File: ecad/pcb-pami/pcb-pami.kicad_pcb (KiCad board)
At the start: 4 copper layers, 95 x 95 mm, 85 parts, among them J1 USB_C_Receptacle_USB2.0_16P, J10 Conn_01x02_Pin, J11 Conn_01x05_Pin, J12 Conn_01x02_Pin, J13 Conn_01x04_Pin, J14 Conn_01x04_Pin, J15 Conn_01x02_Pin, J16 Conn_01x05_Pin, J17 Conn_01x07_Pin, J2 Conn_01x11_Socket, J21 Conn_01x05_Pin, J22 Conn_01x04_Pin, J23 Conn_01x03_Pin, J26 Conn_01x03_Pin, J27 Conn_01x02_Pin, J3 Conn_01x08_Socket, J4 Conn_01x11_Socket, J5 Conn_01x02_Pin, J6 Conn_01x02_Pin, J7 Conn_01x02_Pin, J8 Conn_01x03_Pin, J9 Conn_01x02_Pin, SW1 SW_Push, SW2 SW_Push, U10 MCP23008-xSO, U2 LTC4412xS6, U3 LTC4412xS6, U4 AMS1117-3.3 (UMW), U6 ESP32-S3-WROOM-1, U7 TMC2209_SILENTSTEPSTICK, U8 TMC2209_SILENTSTEPSTICK, U9 TMC2209_SILENTSTEPSTICK

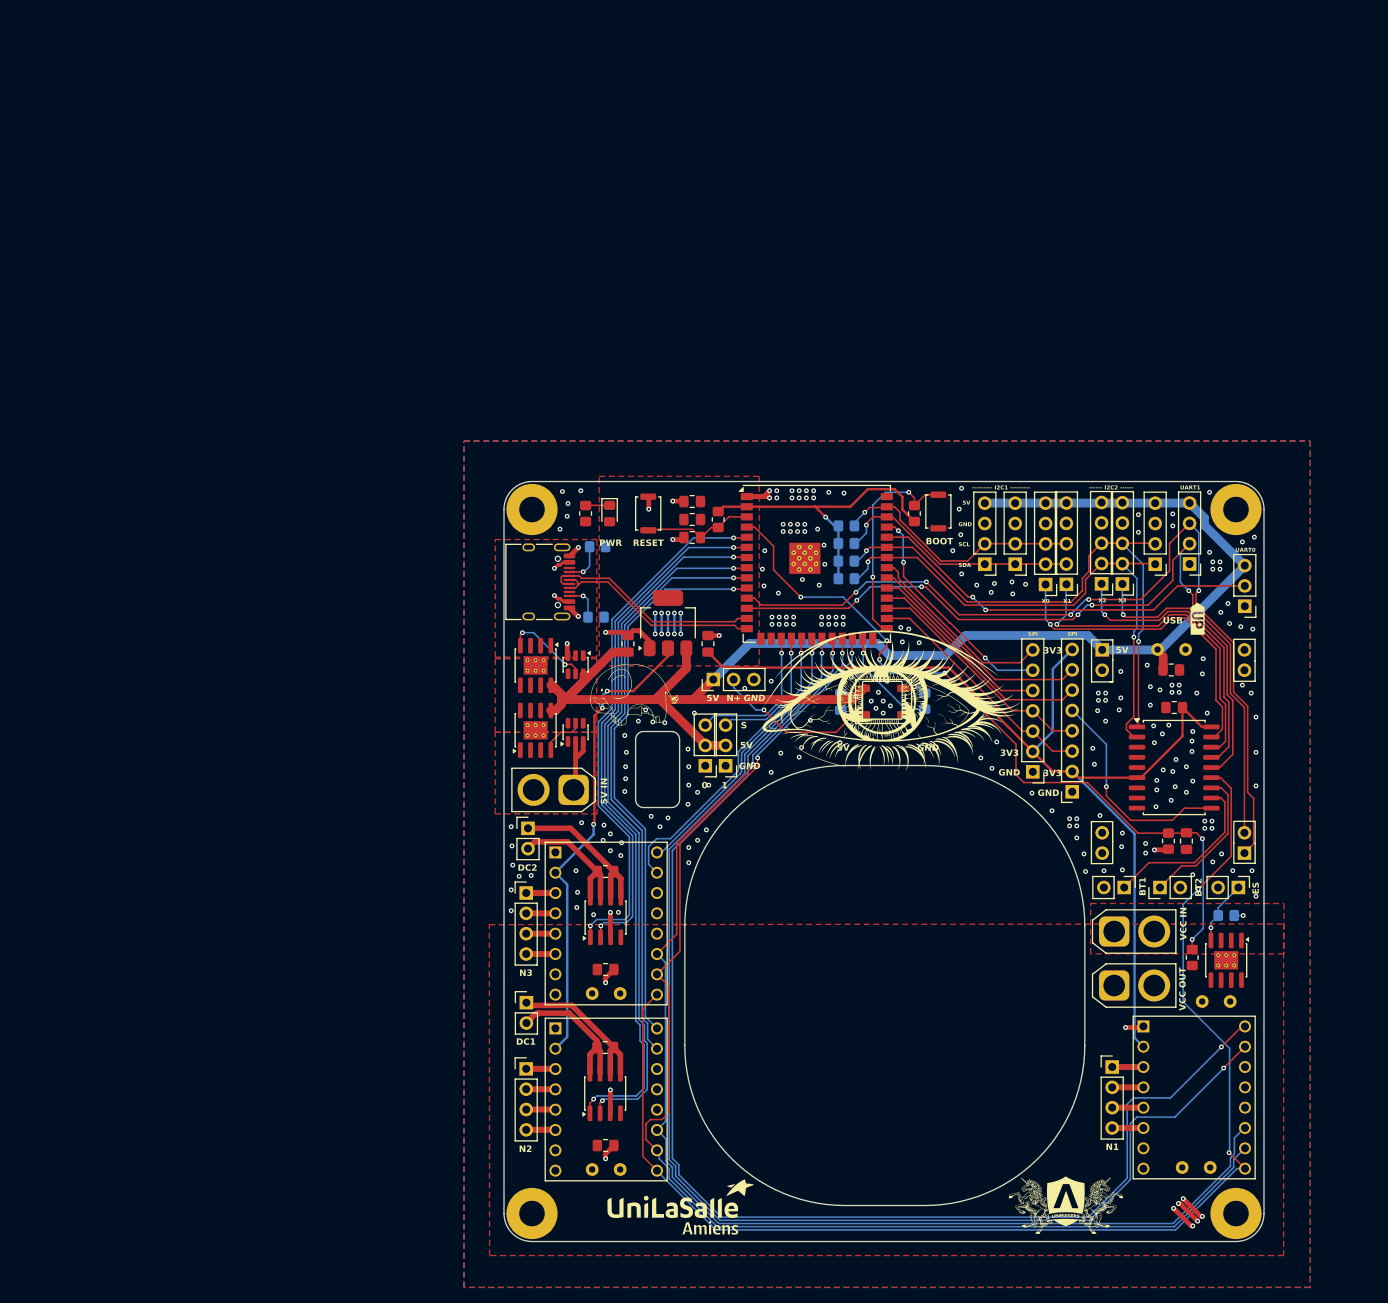
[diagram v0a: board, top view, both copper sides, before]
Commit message: [ECAD] debut nouvelle carte, [FW] generation strat web
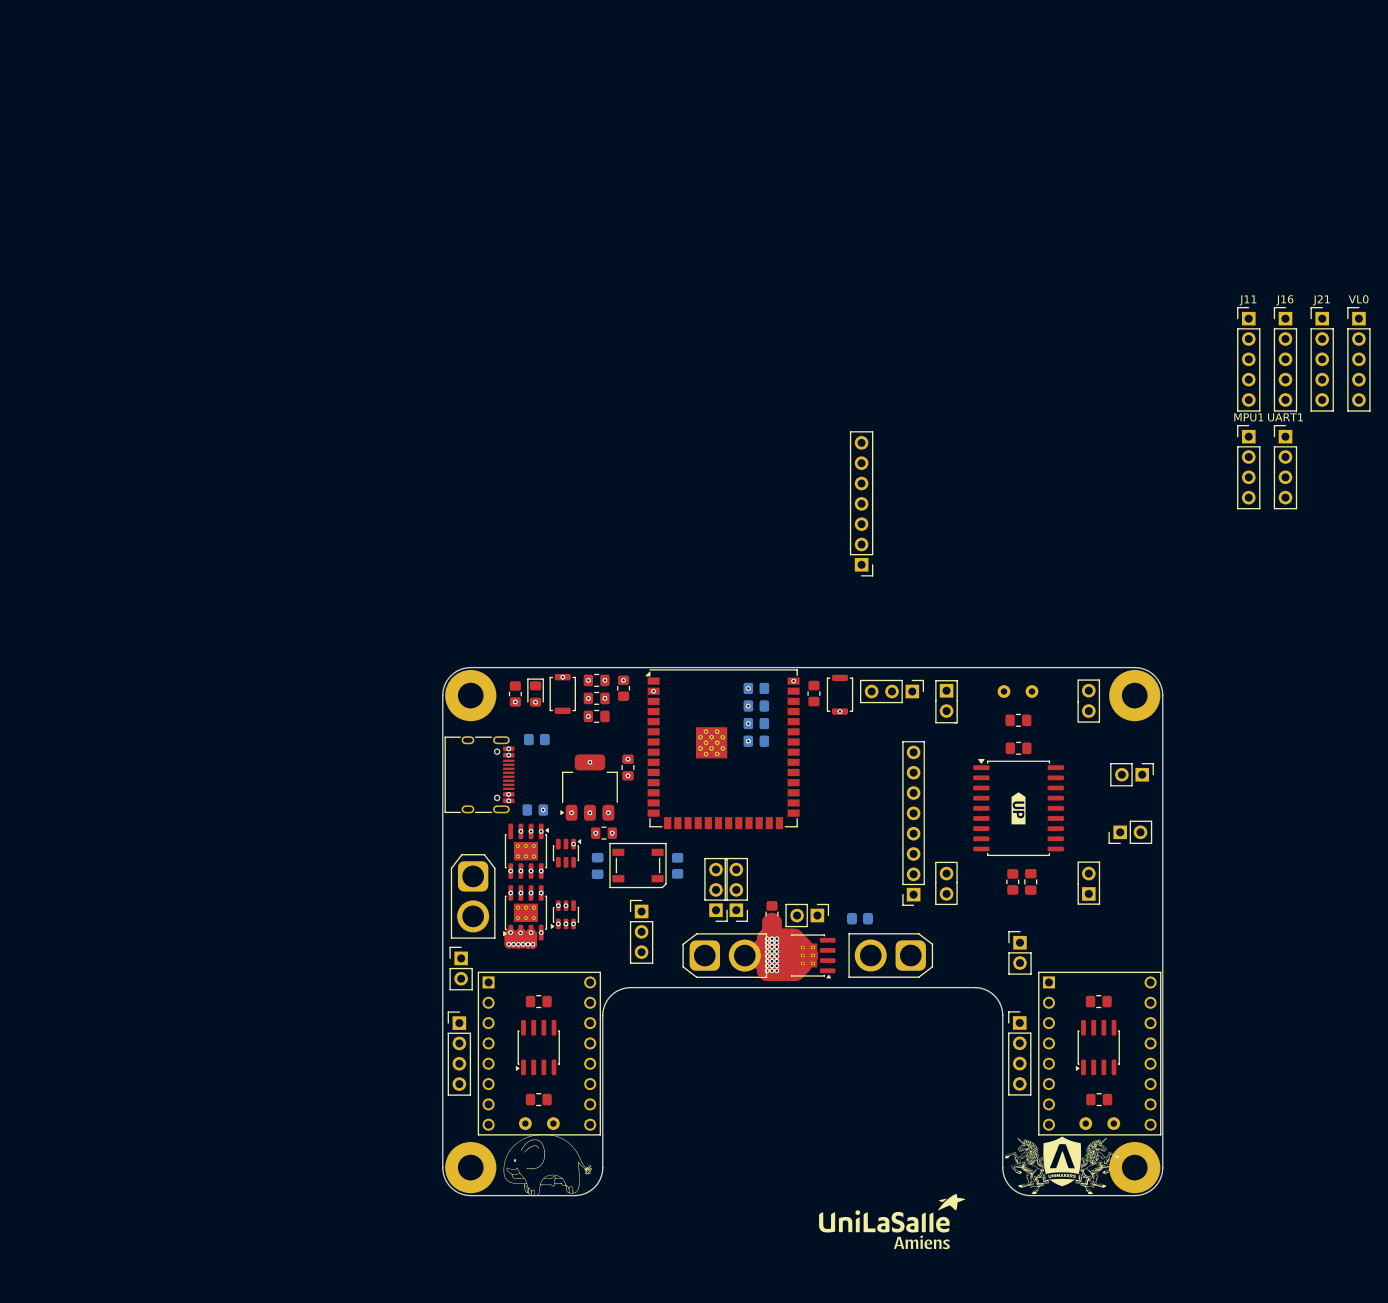
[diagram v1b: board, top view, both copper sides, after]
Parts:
- removed AS1, AS2, J13: Conn_01x04_Pin, Connector_PinHeader_2.54mm:PinHeader_1x04_P2.54mm_Vertical
- removed C3: 100u, Capacitor_THT:C_Radial_D8.0mm_H11.5mm_P3.50mm
- removed C8: 470u, Capacitor_THT:C_Radial_D8.0mm_H11.5mm_P3.50mm
- removed the G*** at (150.8, 71.2)
- removed U7: TMC2209_SILENTSTEPSTICK, TMC2209:MODULE_TMC2209_SILENTSTEPSTICK
- moved H3 111.6 mm to (182.1, 129.5)
- moved H4 98.4 mm to (99.1, 70.5)
- moved H1 66.0 mm to (182.1, 70.5)
- moved J12 62.2 mm to (167.8, 101.4)
- moved C6 62.0 mm to (176.0, 124.0)
- moved J14 62.0 mm to (167.8, 111.4)
- moved U8 62.0 mm to (177.8, 115.3)
- moved C16 62.0 mm to (177.7, 121.0)
- moved C18 62.0 mm to (177.6, 108.8)
- moved U1 62.0 mm to (177.6, 114.5)
- moved G*** 59.8 mm to (108.6, 129.2)
- moved R14 52.8 mm to (136.8, 97.8)
- moved J9 52.7 mm to (142.5, 98.0)
- moved AO4407A4 52.3 mm to (141.3, 103.0), turned to 180 degrees
- moved VL0 51.4 mm to (210.2, 23.4), turned to 0 degrees
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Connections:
- U6 pad 19: STEP3 -> unconnected-(U6-IO11-Pad19)
- U6 pad 20: DIR3 -> unconnected-(U6-IO12-Pad20)
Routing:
- net 3V3: track 239.8 -> 0.00 mm, vias 14 -> 12
- net VCC_5V_GLOBAL: track 198.6 -> 0.00 mm, vias 1 -> 11
- net DIR1: track 163.9 -> 0.00 mm, vias 2 -> 0
- net STEP1: track 162.1 -> 0.00 mm, vias 2 -> 0
- net MS1: track 160.6 -> 0.00 mm, vias 2 -> 0
- net EN: track 159.5 -> 0.00 mm, vias 2 -> 0
- net MS2: track 159.3 -> 0.00 mm, vias 2 -> 0
- net UART1_RX-: track 110.7 -> 0.00 mm, vias 5 -> 0
- net UART1_TX+: track 103.5 -> 0.00 mm, vias 5 -> 0
- net VCC_CALC: track 94.4 -> 0.00 mm, vias 6 -> 0
- net M1_IN2: track 89.2 -> 0.00 mm, vias 2 -> 0
- net M1_IN1: track 87.4 -> 0.00 mm, vias 2 -> 0
- net STEP2: track 73.7 -> 0.00 mm, vias 1 -> 0
- net SCL2: track 70.8 -> 0.00 mm, vias 2 -> 0
- net DIR2: track 70.0 -> 0.00 mm, vias 1 -> 0
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- added copper zone on In1.Cu, net 3V3
- added copper zone on In2.Cu, net GND
- added copper zone on In1.Cu, net VCC_12V
- added copper zone on In1.Cu, net VCC_5V_BUCK
- added copper zone on In1.Cu, net VCC_5V_GLOBAL
- added copper zone on In1.Cu, net VCC_5V_USB
- removed copper zone on F.Cu, net 3V3
- removed copper zone on B.Cu, net GND
- removed copper zone on F.Cu, net GND
- removed copper zone on F.Cu, net VCC_12V
- removed copper zone on F.Cu, net VCC_12V_IN
- removed copper zone on F.Cu, net VCC_5V_BUCK
- removed copper zone on F.Cu, net VCC_5V_GLOBAL
- removed copper zone on F.Cu, net VCC_5V_USB
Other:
- board size 95 x 95 mm -> 90 x 66 mm
- board text removed: "------ I2C2 ------"
- board text removed: "--------- I2C1 ---------"
- board text removed: "0"
- board text removed: "1"
- board text removed: "3V3"
- board text removed: "5V"
- board text removed: "5V IN"
- board text removed: "BOOT"
- board text removed: "BT1"
- board text removed: "BT2"
- board text removed: "DC1"
- board text removed: "DC2"
- board text removed: "ES"
- board text removed: "GND"
- board text removed: "N+"
- board text removed: "N1"
- board text removed: "N2"
- board text removed: "N3"
- board text removed: "PWR"
- board text removed: "RESET"
- board text removed: "S"
- board text removed: "SCL"
- board text removed: "SDA"
- board text removed: "SPI"
- board text removed: "UART0"
- board text removed: "UART1"
- board text removed: "USB"
- board text removed: "VCC IN"
- board text removed: "VCC OUT"
- board text removed: "X0"
- board text removed: "X1"
- board text removed: "X2"
- board text removed: "X3"

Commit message: [ECAD] Préparation V2 carte PAMI
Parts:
- moved VL0 109.5 mm to (101.4, 36.1), turned to 180 degrees
- moved J21 102.5 mm to (103.9, 36.1), turned to 180 degrees
- moved UART0 96.8 mm to (104.5, -13.0)
- moved J16 95.4 mm to (106.4, 36.1), turned to 180 degrees
- moved J11 88.3 mm to (109.0, 36.1), turned to 180 degrees
- moved J7 88.2 mm to (117.3, 25.9)
- moved G*** 85.2 mm to (93.5, 74.2)
- moved MPU1 85.0 mm to (111.5, 33.5), turned to 180 degrees
- moved J5 77.8 mm to (127.5, 25.9)
- moved J3 76.1 mm to (93.8, 49.5), turned to 90 degrees
- moved kibuzzard-6A6F48EA 69.5 mm to (125.4, 29.5)
- moved AO4407A1 65.2 mm to (57.9, 46.0)
- moved AO4407A2 65.2 mm to (57.9, 53.6)
- moved C19 65.2 mm to (59.5, 77.0)
- moved C20 65.2 mm to (59.5, 64.8)
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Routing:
- net VCC_12V: track 64.6 -> 0.00 mm, vias 24 -> 0
- net VCC_5V_BUCK: track 25.3 -> 0.00 mm, vias 10 -> 0
- net USB_P: track 0.00 -> 23.0 mm
- net USB_N: track 0.00 -> 22.9 mm
- net 3V3: track 0.00 -> 12.0 mm, vias 12 -> 5
- net Net-(D1-K): track 0.00 -> 2.54 mm
- net GND: track 0.00 -> 1.46 mm, vias 15 -> 1
- net VCC_5V_USB: vias 6 -> 4
- net VCC_5V_GLOBAL: vias 11 -> 0
- net Net-(AO4407A2-G): vias 2 -> 0
- added copper zone on F.Cu, net 3V3
- added copper zone on In2.Cu, net 3V3
- added copper zone on In1.Cu, net GND
- added copper zone on In2.Cu, net VCC_12V
- added copper zone on In2.Cu, net VCC_5V_BUCK
- added copper zone on F.Cu, net VCC_5V_GLOBAL
- added copper zone on In2.Cu, net VCC_5V_GLOBAL
- added copper zone on F.Cu, net VCC_5V_USB
- added copper zone on In2.Cu, net VCC_5V_USB
- removed copper zone on In1.Cu, net 3V3
- removed copper zone on In2.Cu, net GND
- removed copper zone on In1.Cu, net VCC_12V
- removed copper zone on In1.Cu, net VCC_5V_BUCK
- removed copper zone on In1.Cu, net VCC_5V_GLOBAL
- removed copper zone on In1.Cu, net VCC_5V_USB

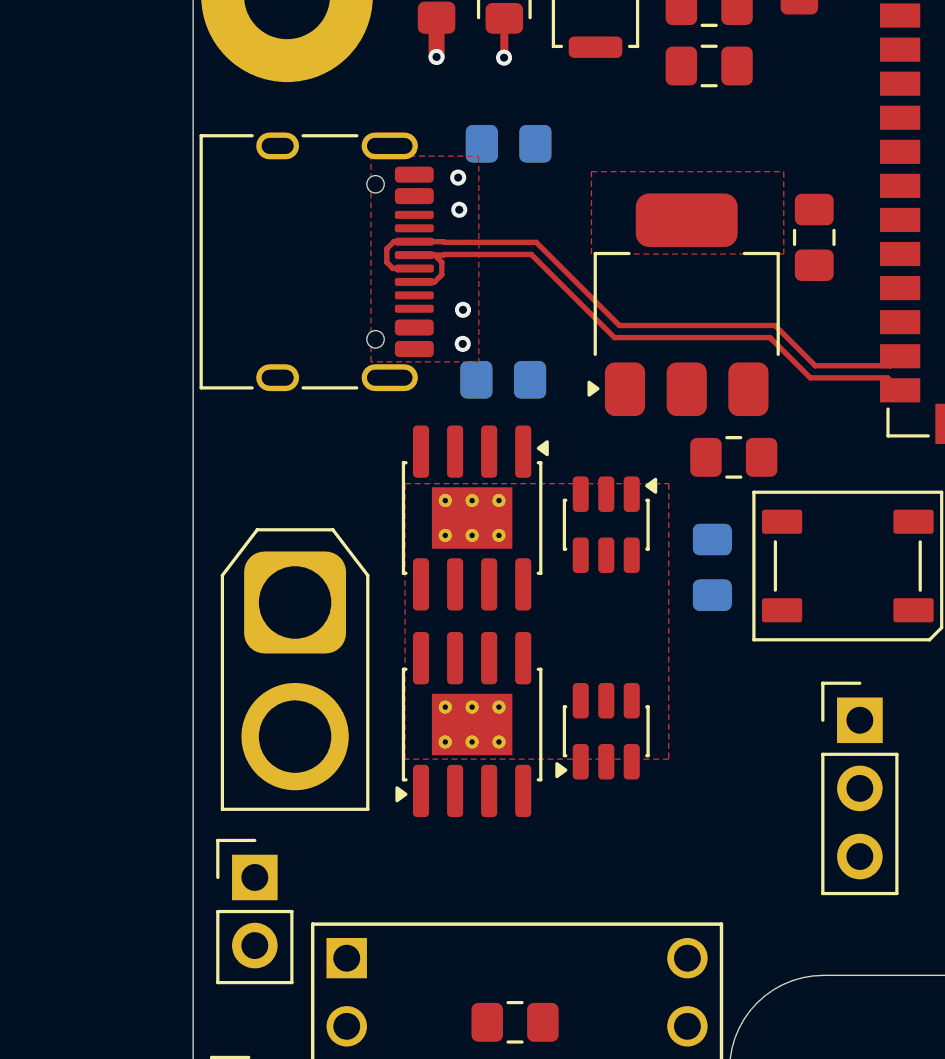
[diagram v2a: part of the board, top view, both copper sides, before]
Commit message: [FW] Evitement & Test PWM Moteur DC
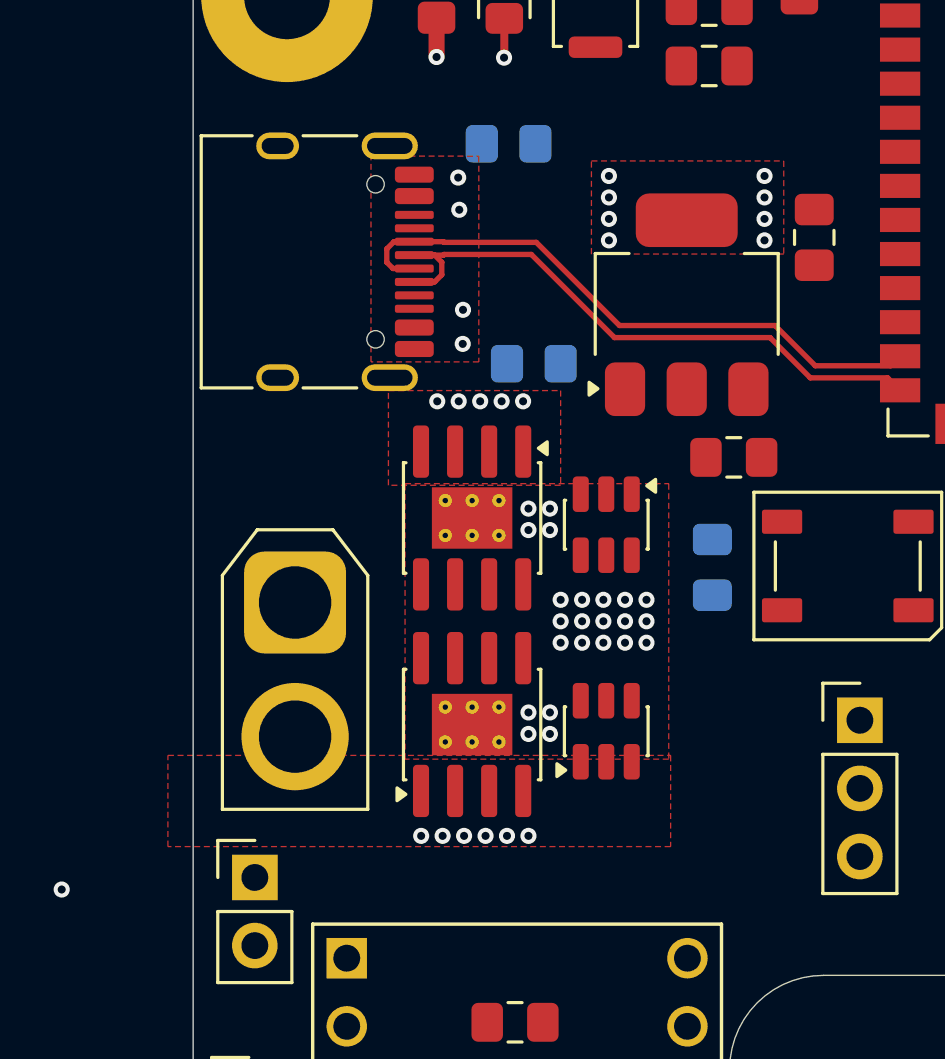
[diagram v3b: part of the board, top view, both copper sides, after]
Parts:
- moved R2 1.29 mm to (60.2, 40.2)
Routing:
- net VCC_5V_USB: vias 4 -> 9
- net VCC_5V_GLOBAL: vias 0 -> 23
- net VCC_5V_BUCK: vias 0 -> 6
- net 3V3: vias 5 -> 13
- net (no net): vias 0 -> 1
- added copper zone on F.Cu, net VCC_5V_BUCK
